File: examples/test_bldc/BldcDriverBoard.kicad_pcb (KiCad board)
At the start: 2 copper layers, 64 parts, among them sw1 5.1mm switch, sw2 5.1mm switch, sw3 5.1mm switch

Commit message: wip layout blocks
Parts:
- moved mcu.crystal.cap_a 118.6 mm to (151.2, 112.2)
- moved mcu.crystal.cap_b 118.6 mm to (156.4, 107.8)
- moved mcu.crystal.package 118.6 mm to (151.8, 108.8)
- moved mcu.ic 118.6 mm to (104.3, 110.4)
- moved mcu.pwr_cap[0] 118.6 mm to (100.9, 117.5)
- moved mcu.pwr_cap[1] 118.6 mm to (109.1, 118.0)
- moved mcu.pwr_cap[2] 118.6 mm to (116.0, 115.5)
- moved mcu.pwr_cap[3] 118.6 mm to (113.1, 118.0)
- moved mcu.swd 118.6 mm to (116.0, 109.5)
- moved mcu.usb_pull 118.6 mm to (112.0, 115.5)
- moved mcu.vdda_cap_0 118.6 mm to (105.1, 117.3)
- moved mcu.vdda_cap_1 118.6 mm to (123.3, 106.0)
- moved curr[3] 106.2 mm to (159.0, 69.0), turned to 90 degrees
- moved curr[1] 105.0 mm to (159.0, 59.0), turned to -90 degrees
- moved curr[2] 92.0 mm to (154.0, 59.0), turned to -90 degrees
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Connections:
- net bldc_drv.(adapter)ic.v3p3.src renamed bldc_drv.nsleep_default.in_default
- net bldc_drv.ic.cpl renamed bldc_drv.cp_cap.neg
- net bldc_drv.pgnd2 renamed bldc_drv.pgnds.2
- net curr[1].sense_out renamed bldc_drv.pgnds.1
- net curr[3].pwr_out renamed bldc_drv.pgnds.3
- net curr_amp[1].(adapter)r2.a.dst renamed curr_amp[1].(adapter)r1.b.src
- net curr_amp[2].r1.b renamed curr_amp[2].(adapter)r1.b.dst
- net curr_amp[3].amp.inn renamed curr_amp[3].r2.a
- net i2c_tp.io.scl renamed i2c.pins.4
- net i2c_tp.io.sda renamed i2c.i2c.sda
- net mcu.crystal.crystal.b renamed mcu.ic.osc.xtal_out
- net mcu.ic.osc.xtal_in renamed mcu.crystal.crystal.a
- net mcu.ic.swd.reset renamed mcu.swd.swd.reset
- net mcu.swd.swd.swclk renamed mcu.ic.swd.swclk
- net mcu.swd.swd.swdio renamed mcu.ic.swd.swdio
- net pd.cc.cc2 renamed usb.cc.cc2
- net usb_esd.usb.dm renamed usb.usb.dm
- bldc pad 1: bldc.pins.1 -> bldc.phases.0
- bldc pad 2: bldc.pins.2 -> bldc_drv.outs.1
- bldc pad 3: bldc.pins.3 -> bldc_drv.outs.2
- bldc_drv.ic pad 22: mcu.gpio.bldc_en3 -> bldc_drv.ens.3
- bldc_drv.ic pad 23: mcu.gpio.bldc_in3 -> mcu.gpio.bldc_in_3
- bldc_drv.ic pad 24: mcu.gpio.bldc_en2 -> mcu.gpio.bldc_en_2
- bldc_drv.ic pad 25: mcu.gpio.bldc_in2 -> mcu.gpio.bldc_in_2
- bldc_drv.ic pad 26: mcu.gpio.bldc_en1 -> bldc_drv.ens.1
- bldc_drv.ic pad 27: mcu.gpio.bldc_in1 -> mcu.gpio.bldc_in_1
- bldc_drv.ic pad 5: bldc.pins.1 -> bldc_drv.outs.1
- bldc_drv.ic pad 8: bldc.pins.2 -> bldc_drv.outs.2
- bldc_drv.ic pad 9: bldc.pins.3 -> bldc.phases.0
- mcu.ic pad 14: mcu.gpio.bldc_in1 -> mcu.gpio.bldc_reset
- mcu.ic pad 15: mcu.gpio.bldc_en3 -> mcu.gpio.sw3
- mcu.ic pad 16: mcu.gpio.bldc_reset -> mcu.gpio.bldc_fault
- mcu.ic pad 17: mcu.gpio.bldc_in2 -> mcu.gpio.sw1
- mcu.ic pad 18: mcu.gpio.bldc_en1 -> mcu.gpio.sw2
- mcu.ic pad 19: mcu.gpio.bldc_en2 -> mcu.gpio.pd_int
- mcu.ic pad 20: mcu.gpio.sw3 -> mcu.gpio.bldc_en_2
- mcu.ic pad 25: mcu.gpio.bldc_fault -> bldc_drv.ens.1
- mcu.ic pad 26: mcu.gpio.sw1 -> bldc_drv.ens.3
- mcu.ic pad 27: mcu.gpio.bldc_in3 -> mcu.gpio.bldc_in_2
- mcu.ic pad 28: mcu.gpio.sw2 -> mcu.gpio.bldc_in_1
- mcu.ic pad 29: mcu.gpio.pd_int -> mcu.gpio.bldc_in_3
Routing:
- net vusb: track 0.00 -> 54.5 mm, vias 0 -> 8
- net gnd: track 0.00 -> 27.3 mm
- net bldc_drv.outs.2: track 0.00 -> 17.8 mm
- net bldc.phases.0: track 0.00 -> 17.6 mm
- net bldc_drv.outs.1: track 0.00 -> 16.1 mm
- net bldc_drv.pgnds.2: track 0.00 -> 14.8 mm
- net bldc_drv.pgnds.1: track 0.00 -> 9.58 mm
- net bldc_drv.pgnds.3: track 0.00 -> 9.31 mm
- net bldc_drv.nsleep_default.in_default: track 0.00 -> 6.49 mm
- net bldc_drv.cp_cap.neg: track 0.00 -> 6.19 mm
- net bldc_drv.ic.cph: track 0.00 -> 5.38 mm
- net bldc_drv.ic.vcp: track 0.00 -> 4.90 mm

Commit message: continued layout
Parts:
- moved bldc 150.8 mm to (182.4, 72.0), turned to 90 degrees
- moved curr_amp[1].r1 110.2 mm to (173.0, 87.0), turned to 180 degrees
- moved curr_amp[1].r2 105.9 mm to (169.0, 87.0), turned to 180 degrees
- moved curr_amp[2].r1 105.6 mm to (180.0, 87.0), turned to 180 degrees
- moved curr_amp[2].r2 100.9 mm to (176.0, 87.0), turned to 180 degrees
- moved curr_amp[2].amp.vdd_cap 100.3 mm to (178.0, 81.0), turned to 180 degrees
- moved curr_amp[2].amp.ic 100.2 mm to (178.0, 84.0)
- moved curr_amp[1].amp.ic 76.5 mm to (171.0, 84.0)
- moved curr_amp[1].amp.vdd_cap 72.6 mm to (171.0, 81.0), turned to 180 degrees
- moved curr_amp[3].r2 50.8 mm to (174.0, 53.0), turned to 0 degrees
- moved pd.vdd_cap[1] 48.3 mm to (69.0, 80.0), turned to 90 degrees
- moved curr_amp[3].amp.ic 44.3 mm to (172.0, 56.0), turned to 180 degrees
- moved curr_amp[3].r1 44.2 mm to (170.0, 53.0), turned to 0 degrees
- moved pd.ic 43.1 mm to (63.0, 80.0), turned to 90 degrees
- moved pd.vdd_cap[0] 43.0 mm to (67.0, 80.0), turned to 90 degrees
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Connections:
- net bldc_drv.ens.1 renamed mcu.gpio.bldc_en_1
- net bldc_drv.ens.3 renamed mcu.gpio.bldc_en_3
- net bldc_drv.ic.cph renamed bldc_drv.cp_cap.pos
- net bldc_drv.ic.vcp renamed bldc_drv.vcp_cap.pos
- net bldc_drv.nsleep_default.in_default renamed bldc_drv.(adapter)ic.v3p3.src
- net curr_amp[1].(adapter)r1.b.src renamed curr_amp[1].(adapter)r2.a.dst
- net curr_amp[2].(adapter)r1.b.dst renamed curr_amp[2].r2.a
- net curr_amp[3].r2.a renamed curr_amp[3].(adapter)r1.b.dst
- net i2c.i2c.sda renamed i2c_tp.io.sda
- net i2c.pins.4 renamed i2c_tp.io.scl
- net mcu.gpio.bldc_in_1 renamed bldc_drv.ins.1
- net mcu.gpio.bldc_in_2 renamed bldc_drv.ins.2
- net mcu.ic.swd.swdio renamed mcu.swd.swd.swdio
- net mcu.swd.swd.reset renamed mcu.ic.swd.reset
- net usb.cc.cc2 renamed pd.cc.cc2
- net usb.usb.dm renamed usb_esd.usb.dm
- net usb_esd.usb.dp renamed usb.usb.dp
- bldc pad 1: bldc.phases.0 -> bldc.pins.1
- bldc pad 2: bldc_drv.outs.1 -> bldc_drv.outs.2
- bldc pad 3: bldc_drv.outs.2 -> bldc.pins.3
- bldc_drv.ic pad 5: bldc_drv.outs.1 -> bldc.pins.1
- bldc_drv.ic pad 9: bldc.phases.0 -> bldc.pins.3
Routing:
- net gnd: track 27.3 -> 111.4 mm, vias 0 -> 27
- net v3v3: track 0.00 -> 79.9 mm, vias 0 -> 7
- net bldc.pins.1: track 0.00 -> 21.4 mm
- net bldc.pins.3: track 0.00 -> 20.0 mm
- net bldc.phases.0: track 17.6 -> 0.00 mm
- net bldc_drv.outs.1: track 16.1 -> 0.00 mm
- net vusb: track 54.5 -> 69.4 mm, vias 8 -> 9
- net bldc_drv.pgnds.1: track 9.58 -> 22.7 mm, vias 0 -> 2
- net bldc_drv.pgnds.3: track 9.31 -> 22.4 mm
- net bldc_drv.pgnds.2: track 14.8 -> 27.9 mm, vias 0 -> 2
- net usb_esd.usb.dm: track 0.00 -> 7.52 mm
- net usb.usb.dp: track 0.00 -> 6.76 mm
- net curr_amp[3].(adapter)r1.b.dst: track 0.00 -> 5.36 mm
- net curr_amp[2].r2.a: track 0.00 -> 5.36 mm
- net curr_amp[1].(adapter)r2.a.dst: track 0.00 -> 5.36 mm
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
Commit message: progress, or looks like it
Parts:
- moved tp_3v3 80.3 mm to (74.0, 63.0)
- moved tp_vusb 64.7 mm to (56.0, 63.0)
- moved tp_gnd 60.5 mm to (56.0, 55.0)
- moved i2c 23.6 mm to (29.4, 54.0), turned to 90 degrees
- moved mcu.usb_pull 13.9 mm to (80.0, 112.0)
- turned prot_3v3 to 90 degrees
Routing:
- net vusb: track 69.4 -> 73.9 mm
- net gnd: track 111.4 -> 115.3 mm, vias 27 -> 26
- net v3v3: track 79.9 -> 82.3 mm, vias 7 -> 8

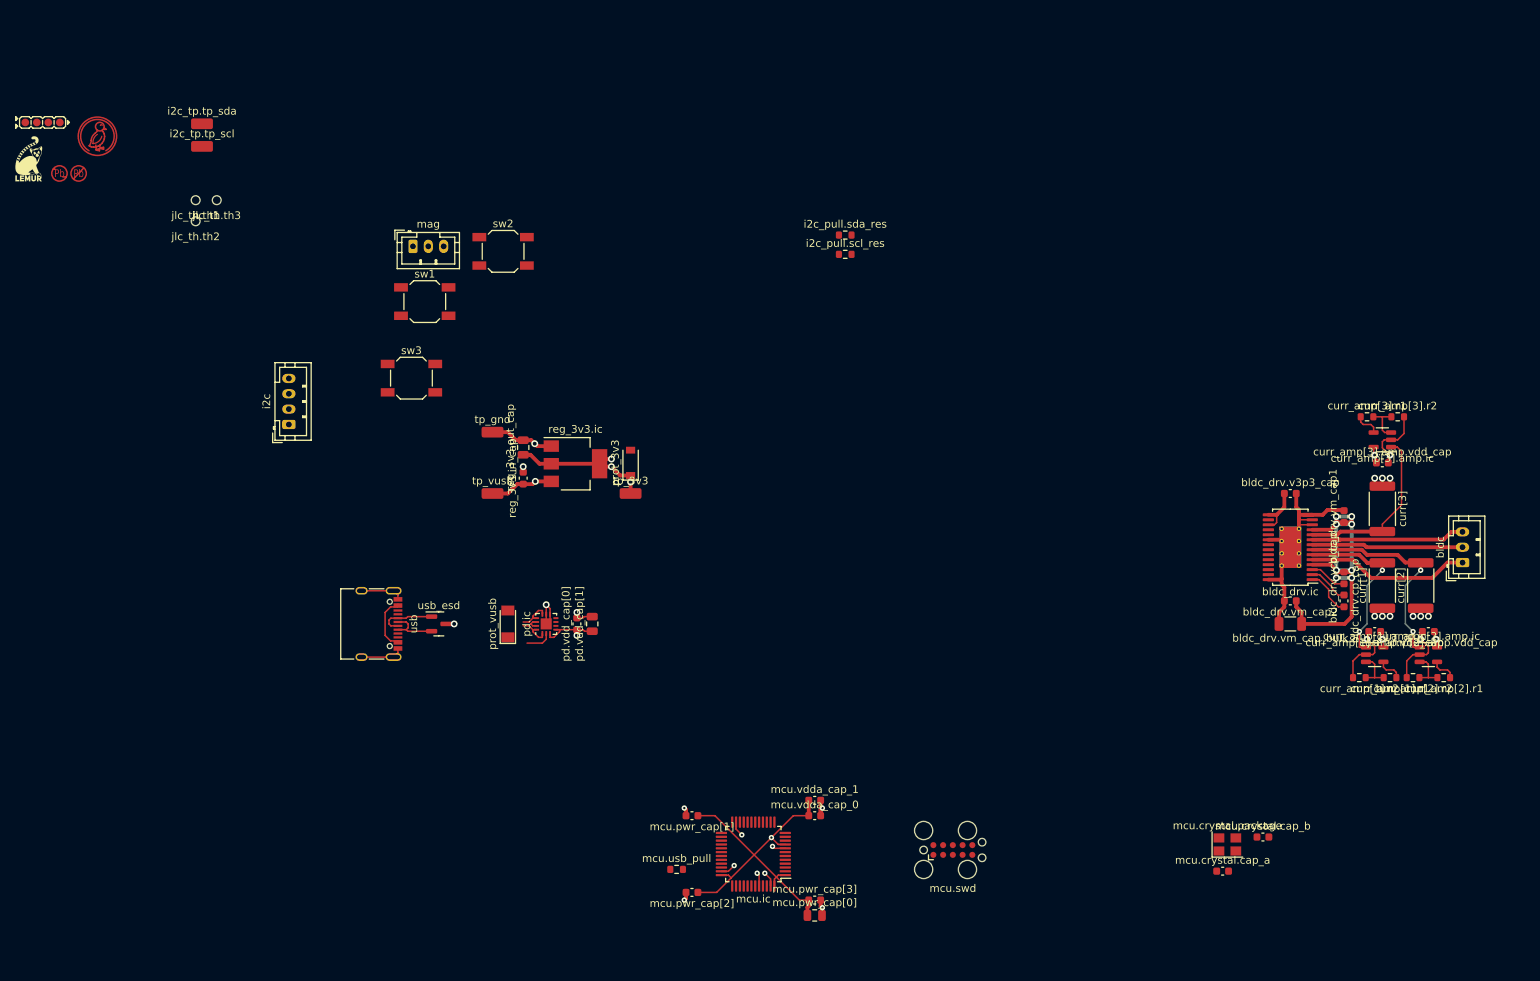
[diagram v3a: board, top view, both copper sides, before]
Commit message: most subblock routing completed
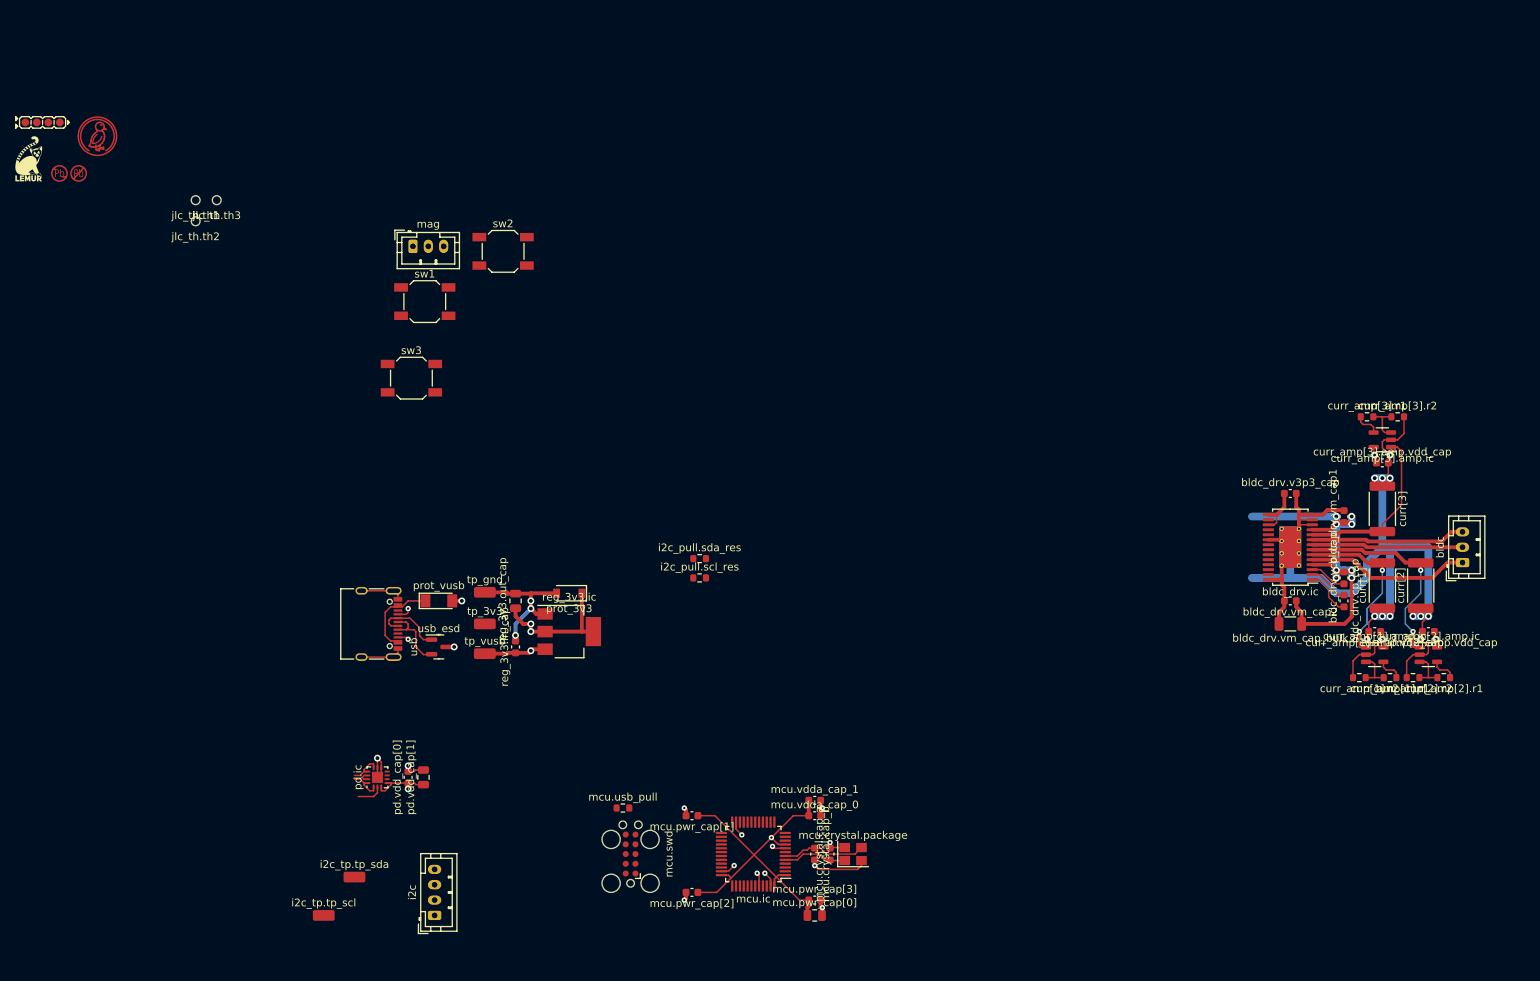
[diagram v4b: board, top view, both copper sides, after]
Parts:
- moved i2c_tp.tp_scl 101.5 mm to (34.0, 118.0)
- moved i2c_tp.tp_sda 100.2 mm to (38.0, 113.0)
- moved i2c 66.8 mm to (48.5, 118.0)
- moved mcu.crystal.cap_b 58.5 mm to (98.0, 110.0), turned to -90 degrees
- moved mcu.crystal.cap_a 51.2 mm to (100.0, 110.0), turned to 90 degrees
- moved mcu.crystal.package 48.8 mm to (103.0, 110.0)
- moved i2c_pull.sda_res 46.3 mm to (83.0, 71.5)
- moved i2c_pull.scl_res 46.3 mm to (83.0, 74.0)
- moved mcu.swd 42.0 mm to (74.0, 110.0), turned to 90 degrees
- moved pd.ic 29.7 mm to (41.0, 100.0)
- moved pd.vdd_cap[0] 29.7 mm to (45.0, 100.0)
- moved pd.vdd_cap[1] 29.7 mm to (47.0, 100.0)
- moved tp_3v3 25.5 mm to (55.0, 80.0)
- moved reg_3v3.in_cap 22.0 mm to (59.0, 83.0)
- moved reg_3v3.ic 21.9 mm to (66.0, 81.0)
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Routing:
- net gnd: track 115.3 -> 207.9 mm, vias 26 -> 30
- net mcu.ic.osc.xtal_out: track 0.00 -> 11.0 mm
- net mcu.crystal.crystal.a: track 0.00 -> 8.40 mm
- net vusb: track 73.9 -> 76.5 mm
- net usb.usb.dp: track 6.76 -> 9.22 mm
- net usb.cc.cc1: track 4.24 -> 6.18 mm, vias 0 -> 1
- net v3v3: track 82.3 -> 80.4 mm, vias 8 -> 7
- net usb_esd.usb.dm: track 7.52 -> 9.21 mm
- net pd.cc.cc2: track 4.24 -> 5.68 mm, vias 0 -> 1

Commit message: Update BldcDriverBoard.kicad_pcb
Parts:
- moved mag 151.6 mm to (182.0, 97.0), turned to 90 degrees
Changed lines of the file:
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@@
   )
   (footprint "Connector_JST:JST_PH_B3B-PH-K_1x03_P2.00mm_Vertical" (layer "F.Cu")
-    (at 45.63 30.78)
+    (at 182 97 90)
     (descr "JST PH series connector, B3B-PH-K (http://www.jst-mfg.com/product/pdf/eng/ePH.pdf), generated with kicad-footprint-generator")
     (tags "connector JST PH side entry")
@@
     (property "edg_short_path" "mag")
     (attr through_hole)
-    (fp_text reference "mag" (at 2 -2.9) (layer "F.SilkS")
+    (fp_text reference "mag" (at 2 -2.9 90) (layer "F.SilkS")
       (effects (font (size 1 1) (thickness 0.15)))
     )
-    (fp_text value "B3B-PH-K (JST)" (at 2 4) (layer "F.Fab")
+    (fp_text value "B3B-PH-K (JST)" (at 2 4 90) (layer "F.Fab")
       (effects (font (size 1 1) (thickness 0.15)))
     )
-    (fp_text user "${REFERENCE}" (at 2 1.5) (layer "F.Fab")
+    (fp_text user "${REFERENCE}" (at 2 1.5 90) (layer "F.Fab")
       (effects (font (size 1 1) (thickness 0.15)))
     )
@@
     (fp_line (start 5.95 -1.7) (end -1.95 -1.7) (layer "F.Fab") (width 0.1))
     (fp_line (start -1.95 -1.7) (end -1.95 2.8) (layer "F.Fab") (width 0.1))
-    (pad "1" thru_hole roundrect (at 0 0) (size 1.2 1.75) (drill 0.75) (layers *.Cu *.Mask) (roundrect_rratio 0.208333)
+    (pad "1" thru_hole roundrect (at 0 0 90) (size 1.2 1.75) (drill 0.75) (layers *.Cu *.Mask) (roundrect_rratio 0.208333)
       (net 2 "v3v3"))
-    (pad "2" thru_hole oval (at 2 0) (size 1.2 1.75) (drill 0.75) (layers *.Cu *.Mask)
+    (pad "2" thru_hole oval (at 2 0 90) (size 1.2 1.75) (drill 0.75) (layers *.Cu *.Mask)
       (net 44 "mag.pins.2"))
-    (pad "3" thru_hole oval (at 4 0) (size 1.2 1.75) (drill 0.75) (layers *.Cu *.Mask)
+    (pad "3" thru_hole oval (at 4 0 90) (size 1.2 1.75) (drill 0.75) (layers *.Cu *.Mask)
       (net 1 "gnd"))
     (model "${KICAD6_3DMODEL_DIR}/Connector_JST.3dshapes/JST_PH_B3B-PH-K_1x03_P2.00mm_Vertical.wrl"

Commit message: towards a pcb, slowly
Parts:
- added conv.in_high_switch.drv: AOD403 (Alpha & Omega Semicon) - 30V 15A 6m?@20V,20A 2.5W 3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, Package_TO_SOT_SMD:TO-252-2, F.Cu at (148.0, 97.5)
- added conv.in_high_switch.pre: 2N7002 (Changjiang Electronics Tech (CJ)) - 60V 115mA 200mW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, Package_TO_SOT_SMD:SOT-23, F.Cu at (139.0, 96.0)
- added conv.in_high_switch.pull: , Resistor_SMD:R_0603_1608Metric, F.Cu at (139.0, 100.0)
- added conv.in_low_diode: SS34 (MDD?Microdiode Electronics?) - 40V 550mV@3A 3A SMA(DO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, Diode_SMD:D_SMA, F.Cu at (147.0, 105.0)
- added conv.out_high_diode: SS34 (MDD?Microdiode Electronics?) - 40V 550mV@3A 3A SMA(DO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, Diode_SMD:D_SMA, F.Cu at (169.0, 95.0)
- added conv.out_low_switch: HSL6008 (HUASHUO) - 60V 2.8A 100m?@10V,2.5A 1.5W 2.5V@250?A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, Package_TO_SOT_SMD:SOT-223-3_TabPin2, F.Cu at (169.0, 103.0)
- added conv.power_path.in_cap.c[0]: , Capacitor_SMD:C_1206_3216Metric, F.Cu at (139.0, 103.0)
- added conv.power_path.in_cap.c[1]: , Capacitor_SMD:C_1206_3216Metric, F.Cu at (139.0, 106.0)
- added conv.power_path.inductor: , Inductor_SMD:L_Taiyo-Yuden_NR-60xx, F.Cu at (159.0, 100.0)
- added conv.power_path.out_cap.c[0]: , Capacitor_SMD:C_0805_2012Metric, F.Cu at (177.0, 94.0)
- added conv.power_path.out_cap.c[1]: , Capacitor_SMD:C_0805_2012Metric, F.Cu at (177.0, 97.0)
- added conv.power_path.out_cap.c[2]: , Capacitor_SMD:C_0805_2012Metric, F.Cu at (177.0, 100.0)
- added conv.power_path.out_cap.c[3]: , Capacitor_SMD:C_0805_2012Metric, F.Cu at (177.0, 103.0)
- added conv.power_path.out_cap.c[4]: , Capacitor_SMD:C_0805_2012Metric, F.Cu at (177.0, 106.0)
- added conv_out: B2B-PH-K (JST), Connector_JST:JST_PH_B2B-PH-K_1x02_P2.00mm_Vertical, F.Cu at (183.0, 100.0)
- added conv_sense.bottom_res: , Resistor_SMD:R_0603_1608Metric, F.Cu at (167.0, 91.0)
- added conv_sense.top_res: , Resistor_SMD:R_0603_1608Metric, F.Cu at (171.0, 91.0)
- moved jlc_th.th2 184.3 mm to (184.0, 106.0)
- moved jlc_th.th3 168.4 mm to (184.0, 63.0)
- moved jlc_th.th1 123.3 mm to (110.0, 106.0)
- moved pd.ic 85.4 mm to (121.0, 70.2)
- moved pd.vdd_cap[0] 85.4 mm to (125.0, 70.2)
- moved pd.vdd_cap[1] 85.4 mm to (127.0, 70.2)
- moved duck 82.1 mm to (53.7, 82.2)
- moved id 82.1 mm to (46.5, 80.3)
- moved leadfree 82.1 mm to (50.0, 87.0)
- moved lemur 82.1 mm to (44.7, 85.1)
- moved mcu.pwr_cap[0] 75.7 mm to (149.0, 62.0), turned to 90 degrees
- moved prot_vusb 75.3 mm to (121.0, 55.0)
- moved usb 75.3 mm to (112.0, 58.0)
- moved usb_esd 75.3 mm to (121.0, 61.0)
- moved mcu.pwr_cap[2] 73.9 mm to (146.0, 78.0), turned to -90 degrees
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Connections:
- net bldc.pins.1 renamed bldc_drv.outs.1
- net bldc.pins.3 renamed bldc.phases.3
- net bldc_drv.vcp_cap.pos renamed bldc_drv.ic.vcp
- net curr_amp[1].(adapter)r2.a.dst renamed curr_amp[1].(adapter)r1.b.dst
- net curr_amp[2].r2.a renamed curr_amp[2].(adapter)r1.b.src
- net curr_amp[3].(adapter)r1.b.dst renamed curr_amp[3].(adapter)r2.a.dst
- net i2c_tp.io.sda renamed i2c.i2c.sda
- net mcu.adc.curr1 renamed mcu.adc.curr_1
- net mcu.adc.curr2 renamed mcu.adc.curr_2
- net mcu.adc.curr3 renamed mcu.adc.curr_3
- net mcu.crystal.crystal.a renamed mcu.ic.osc.xtal_in
- net mcu.ic.swd.swclk renamed mcu.swd.swd.swclk
- net mcu.ic.swd.swo renamed mcu.swd.swd.swo
- net usb.usb.dp renamed usb_esd.usb.dp
- net usb_esd.usb.dm renamed usb.usb.dm
- bldc_drv.ic pad 22: mcu.gpio.bldc_en_3 -> bldc_drv.ens.3
- bldc_drv.ic pad 23: mcu.gpio.bldc_in_3 -> bldc_drv.ins.3
- bldc_drv.ic pad 25: bldc_drv.ins.2 -> mcu.gpio.bldc_in_2
- mcu.ic pad 14: mcu.gpio.bldc_reset -> mcu.adc.conv_sense
- mcu.ic pad 15: mcu.gpio.sw3 -> mcu.gpio.boost_pwm
- mcu.ic pad 16: mcu.gpio.bldc_fault -> mcu.gpio.bldc_reset
- mcu.ic pad 17: mcu.gpio.sw1 -> mcu.gpio.buck_pwm
- mcu.ic pad 18: mcu.gpio.sw2 -> mcu.gpio.sw3
- mcu.ic pad 19: mcu.gpio.pd_int -> mcu.gpio.bldc_fault
- mcu.ic pad 20: mcu.gpio.bldc_en_2 -> mcu.gpio.sw1
- mcu.ic pad 25: mcu.gpio.bldc_en_1 -> mcu.gpio.sw2
- mcu.ic pad 26: mcu.gpio.bldc_en_3 -> mcu.gpio.pd_int
- mcu.ic pad 27: bldc_drv.ins.2 -> mcu.gpio.bldc_en_2
- mcu.ic pad 28: bldc_drv.ins.1 -> mcu.gpio.bldc_en_1
- mcu.ic pad 29: mcu.gpio.bldc_in_3 -> bldc_drv.ens.3
- mcu.ic pad 30: (no net) -> mcu.gpio.bldc_in_2
- mcu.ic pad 31: (no net) -> bldc_drv.ins.1
- mcu.ic pad 38: (no net) -> bldc_drv.ins.3
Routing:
- net conv_out.pins.2: track 0.00 -> 22.7 mm
- net conv.(adapter)out_high_diode.anode.dst: track 0.00 -> 18.6 mm
- net vusb: track 76.5 -> 94.3 mm, vias 9 -> 11
- net conv.(adapter)in_high_switch.output.dst: track 0.00 -> 15.6 mm
- net usb.cc.cc1: track 6.18 -> 21.0 mm, vias 1 -> 2
- net gnd: track 207.9 -> 222.2 mm, vias 30 -> 39
- net pd.cc.cc2: track 5.68 -> 16.6 mm
- net conv.in_high_switch.(adapter)pull.b.dst: track 0.00 -> 8.24 mm
- net mcu.adc.conv_sense: track 0.00 -> 2.35 mm
- net usb_esd.usb.dp: track 9.22 -> 11.3 mm
- net v3v3: track 80.4 -> 81.6 mm, vias 7 -> 8
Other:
- board outline added: 78 x 57 mm
